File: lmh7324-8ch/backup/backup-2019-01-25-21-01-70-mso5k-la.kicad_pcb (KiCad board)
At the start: 4 copper layers, 155 parts, among them IC201 lmh7324, IC301 lmh7324, IC401 lmh7324, IC501 lmh7324, J101 output, J102 input

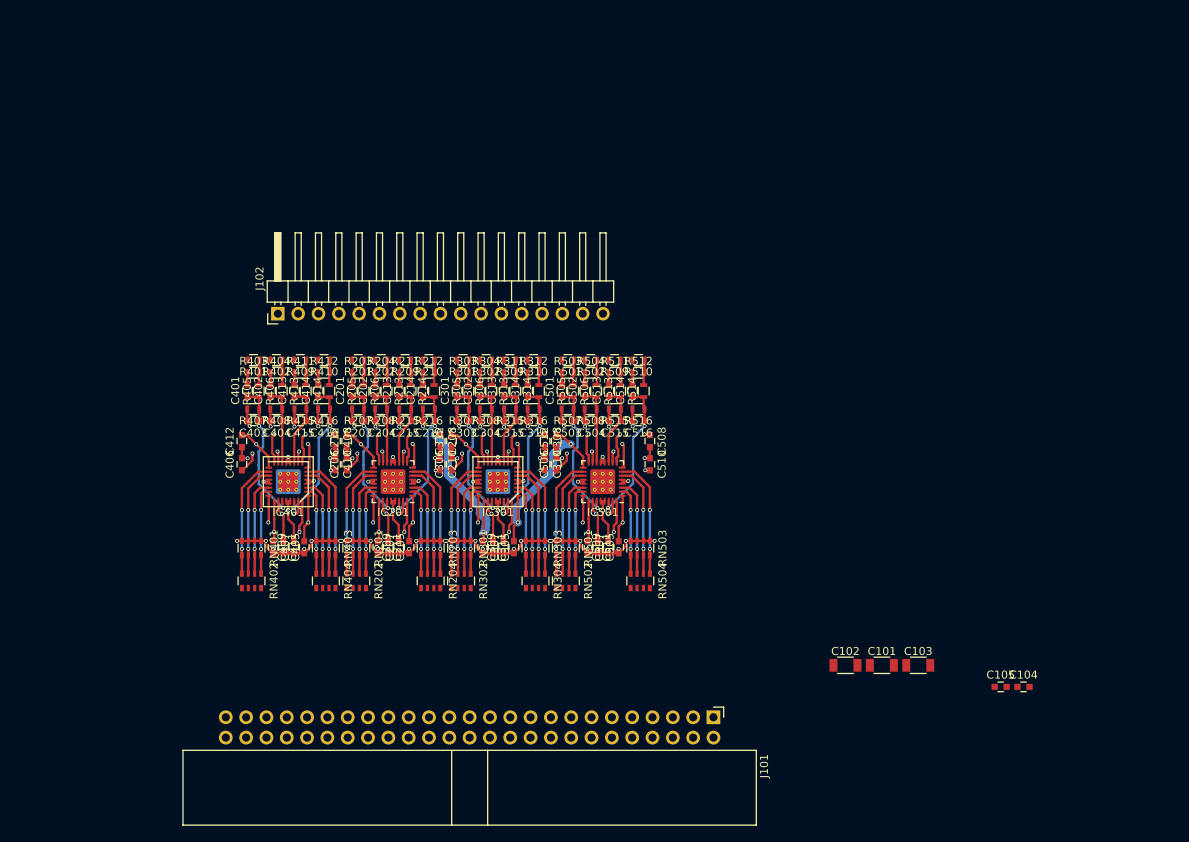
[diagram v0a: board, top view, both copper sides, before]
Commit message: Laid out the 8ch LMH7324 version and added a threshold display too
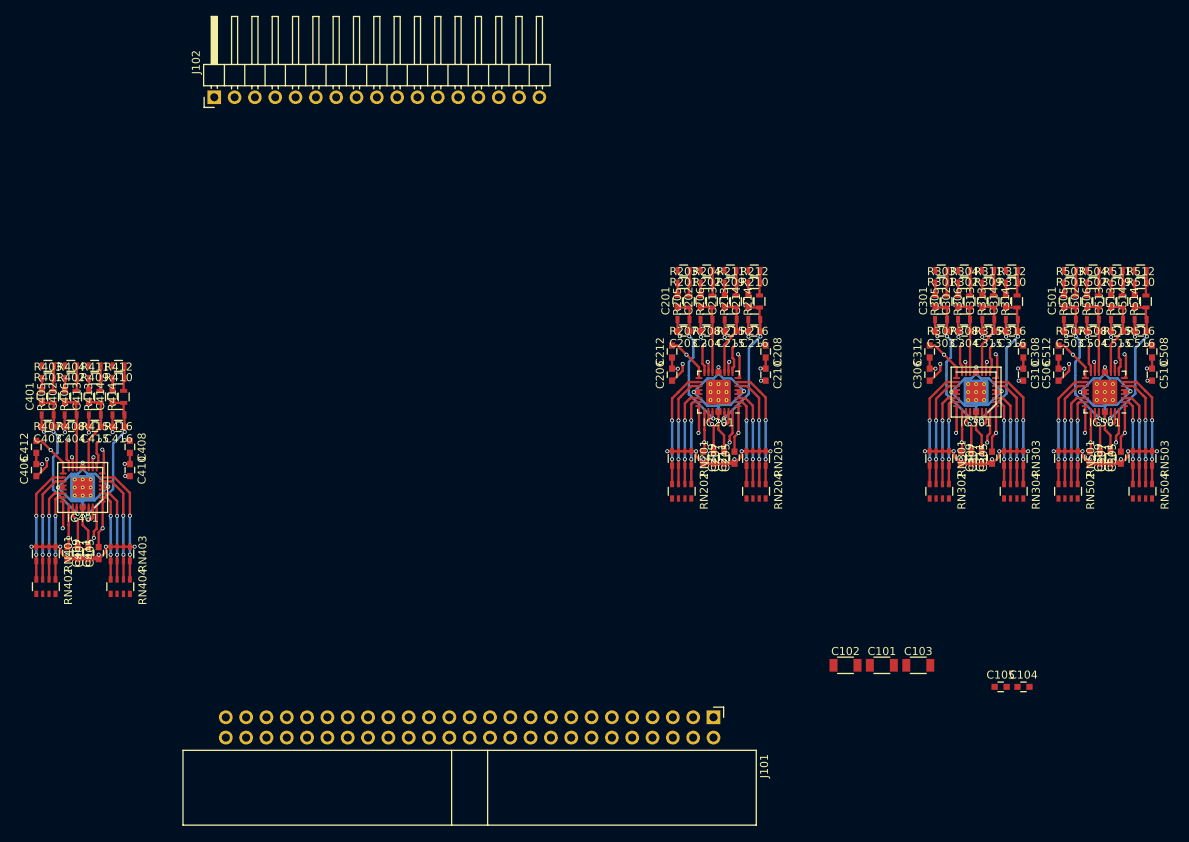
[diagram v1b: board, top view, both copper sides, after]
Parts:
- moved C501 63.8 mm to (155.4, 144.8)
- moved C502 63.8 mm to (158.3, 144.8)
- moved C505 63.8 mm to (159.9, 164.4)
- moved C507 63.8 mm to (158.6, 164.4)
- moved C510 63.8 mm to (166.4, 154.1)
- moved C511 63.8 mm to (162.5, 164.4)
- moved C513 63.8 mm to (161.3, 144.8)
- moved C514 63.8 mm to (164.2, 144.8)
- moved C503 63.8 mm to (156.2, 148.7)
- moved C504 63.8 mm to (159.1, 148.7)
- moved C506 63.8 mm to (154.7, 154.1)
- moved C508 63.8 mm to (166.4, 151.2)
- moved C509 63.8 mm to (161.2, 164.4)
- moved C515 63.8 mm to (162.1, 148.7)
- moved C516 63.8 mm to (165.0, 148.7)
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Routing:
- net -2V5: track 142.0 -> 200.5 mm
- net +4V: track 189.7 -> 174.7 mm
- net +2V5: track 192.5 -> 179.2 mm
- net Vref_0-7: track 69.3 -> 80.7 mm
- net Vref_8-15: track 72.0 -> 80.7 mm
- removed copper zone on 3_Misc, net -2V5
